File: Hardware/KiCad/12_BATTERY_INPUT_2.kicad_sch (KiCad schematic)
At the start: 0 parts

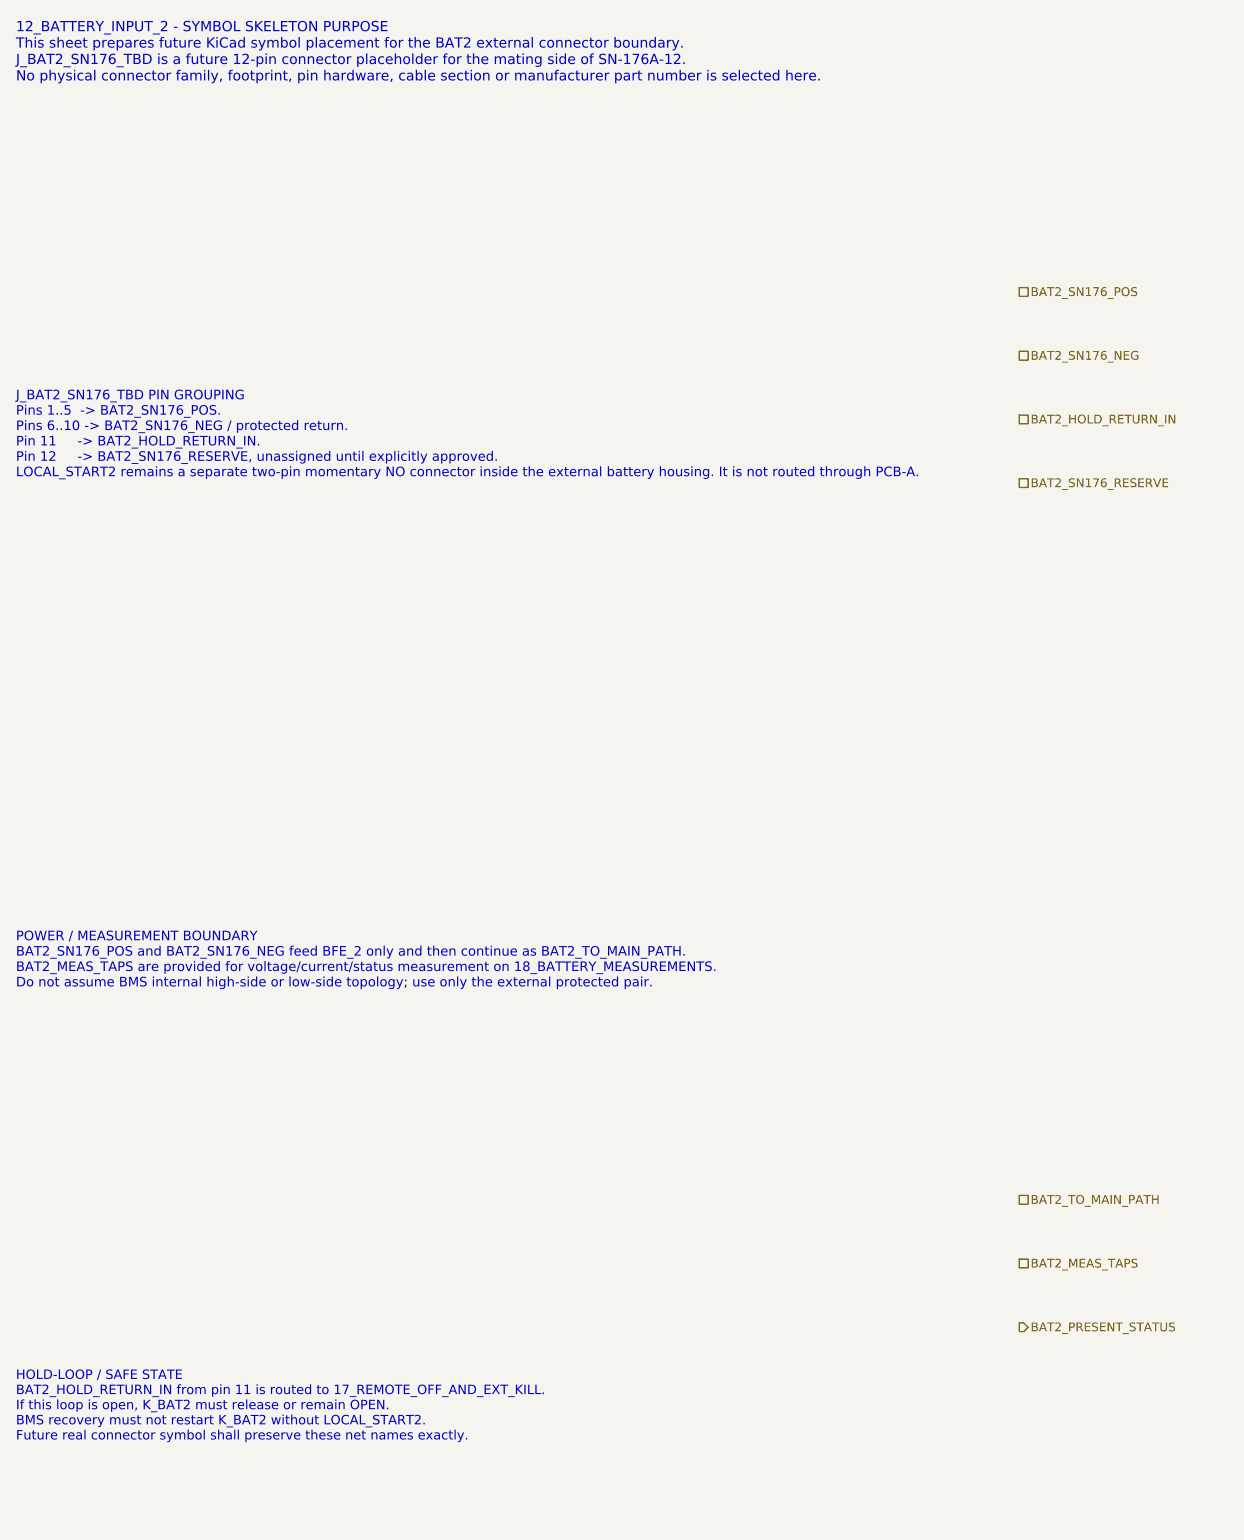
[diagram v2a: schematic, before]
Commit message: hardware: align BAT2 balance and status interfaces
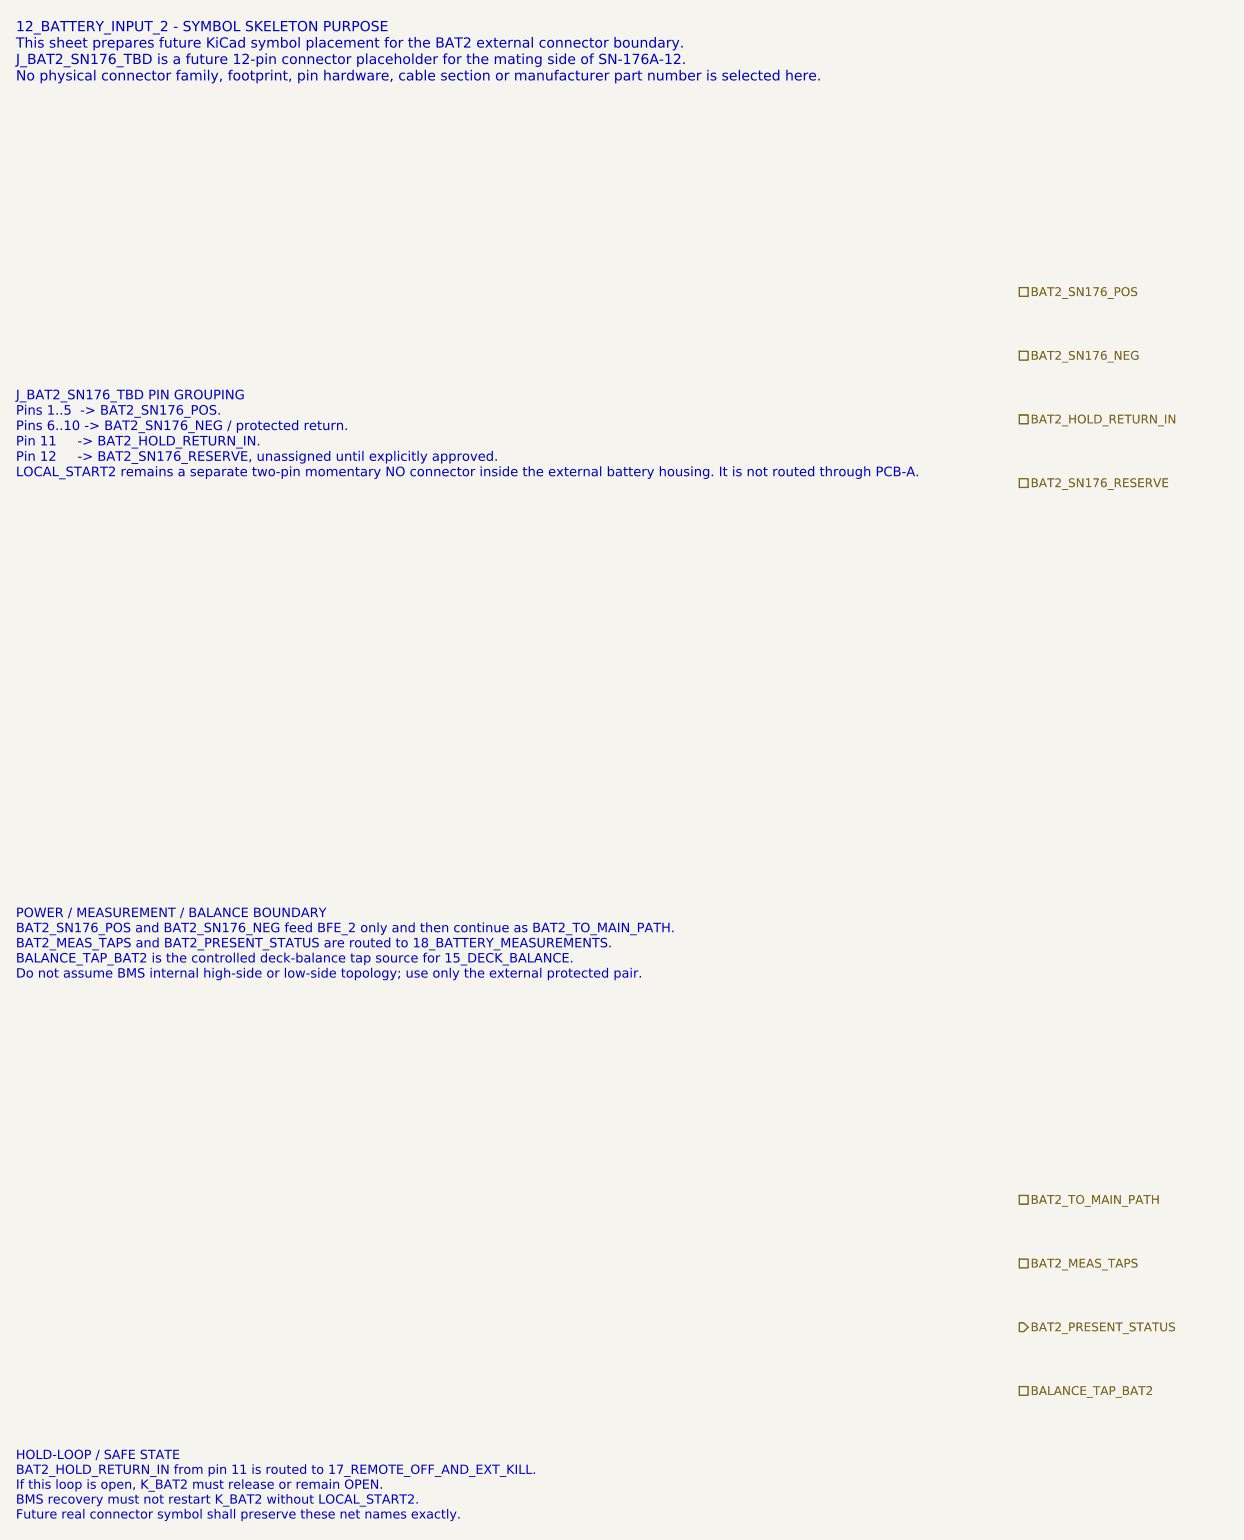
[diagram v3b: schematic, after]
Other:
- note added: "POWER / MEASUREMENT / BALANCE BOUNDARY BAT2_SN176_POS and BAT2_SN176_NEG feed BFE_2 only and then continue as BAT2_TO_MAIN_PATH. BAT2_MEAS_TAPS and BAT2_PRESENT_STATUS are routed to 18_BATTERY_MEASUREMENTS. BALANCE_TAP_BAT2 is the controlled deck-balance tap source for 15_DECK_BALANCE. Do not assume BMS internal high-side or low-side topology; use only the external protected pair."
- note removed: "POWER / MEASUREMENT BOUNDARY BAT2_SN176_POS and BAT2_SN176_NEG feed BFE_2 only and then continue as BAT2_TO_MAIN_PATH. BAT2_MEAS_TAPS are provided for voltage/current/status measurement on 18_BATTERY_MEASUREMENTS. Do not assume BMS internal high-side or low-side topology; use only the external protected pair."
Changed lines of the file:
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@@
 		(title "12_BATTERY_INPUT_2 - BFE input from AKB_2")
 		(date "2026-07-15")
-		(rev "C0")
+		(rev "C1")
 		(company "Gonoboben/plataVM")
-		(comment 1 "Symbol skeleton: BAT2 SN-176A-12 boundary and future connector placement zones")
+		(comment 1 "Interface consistency: BAT2 connector boundary, balance tap and status")
 		(comment 2 "Symmetric to 11_BATTERY_INPUT_1; no connector family or footprint selected")
 	)
@@
 		(uuid "bfe-symbol-00000012-0000-4000-8000-000000000102")
 	)
-	(text "POWER / MEASUREMENT BOUNDARY\nBAT2_SN176_POS and BAT2_SN176_NEG feed BFE_2 only and then continue as BAT2_TO_MAIN_PATH.\nBAT2_MEAS_TAPS are provided for voltage/current/status measurement on 18_BATTERY_MEASUREMENTS.\nDo not assume BMS internal high-side or low-side topology; use only the external protected pair."
+	(text "POWER / MEASUREMENT / BALANCE BOUNDARY\nBAT2_SN176_POS and BAT2_SN176_NEG feed BFE_2 only and then continue as BAT2_TO_MAIN_PATH.\nBAT2_MEAS_TAPS and BAT2_PRESENT_STATUS are routed to 18_BATTERY_MEASUREMENTS.\nBALANCE_TAP_BAT2 is the controlled deck-balance tap source for 15_DECK_BALANCE.\nDo not assume BMS internal high-side or low-side topology; use only the external protected pair."
 		(exclude_from_sim no)
-		(at 12 128 0)
-		(effects (font (size 1.20 1.20)) (justify left))
+		(at 12 126 0)
+		(effects (font (size 1.18 1.18)) (justify left))
 		(uuid "bfe-symbol-00000012-0000-4000-8000-000000000103")
 	)
 	(text "HOLD-LOOP / SAFE STATE\nBAT2_HOLD_RETURN_IN from pin 11 is routed to 17_REMOTE_OFF_AND_EXT_KILL.\nIf this loop is open, K_BAT2 must release or remain OPEN.\nBMS recovery must not restart K_BAT2 without LOCAL_START2.\nFuture real connector symbol shall preserve these net names exactly."
 		(exclude_from_sim no)
-		(at 12 184 0)
-		(effects (font (size 1.18 1.18)) (justify left))
+		(at 12 194 0)
+		(effects (font (size 1.16 1.16)) (justify left))
 		(uuid "bfe-symbol-00000012-0000-4000-8000-000000000104")
 	)
@@
 	(hierarchical_label "BAT2_MEAS_TAPS" (shape passive) (exclude_from_sim no) (at 138 166 0) (effects (font (size 1.1 1.1)) (justify left)) (uuid "bfe-symbol-00000012-0000-4000-8000-000000000206"))
 	(hierarchical_label "BAT2_PRESENT_STATUS" (shape output) (exclude_from_sim no) (at 138 174 0) (effects (font (size 1.1 1.1)) (justify left)) (uuid "bfe-symbol-00000012-0000-4000-8000-000000000207"))
+	(hierarchical_label "BALANCE_TAP_BAT2" (shape passive) (exclude_from_sim no) (at 138 182 0) (effects (font (size 1.1 1.1)) (justify left)) (uuid "bfe-symbol-00000012-0000-4000-8000-000000000208"))
 )
